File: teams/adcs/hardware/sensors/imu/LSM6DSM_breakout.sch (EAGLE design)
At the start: 6 parts

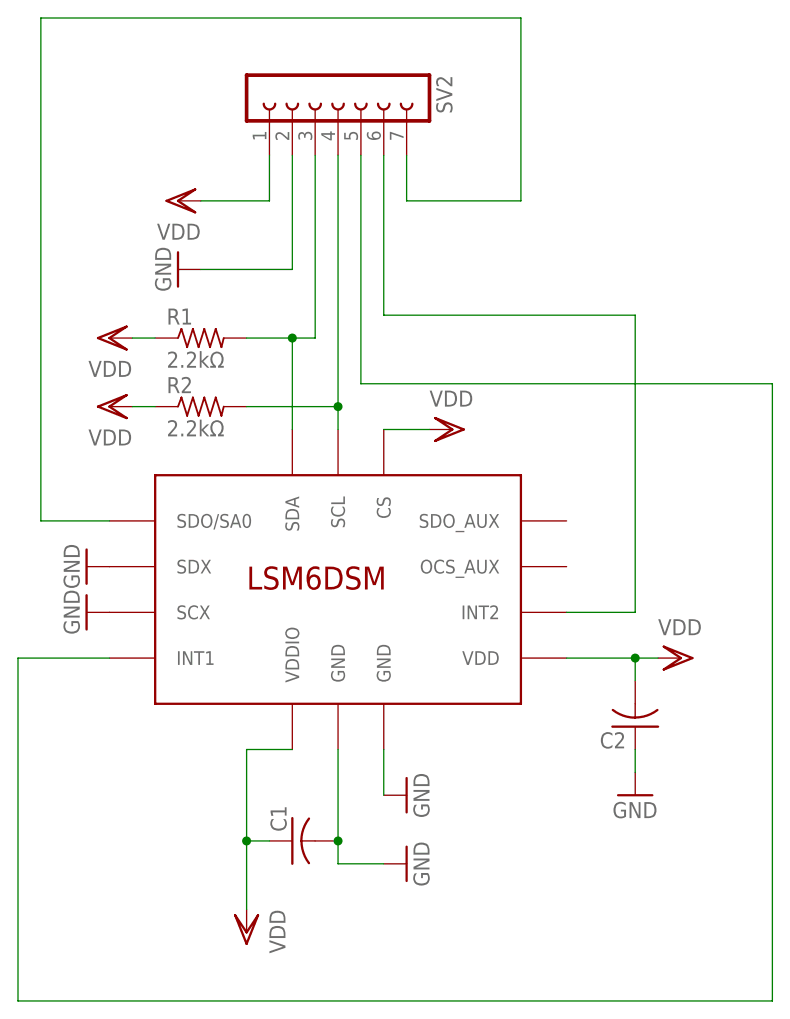
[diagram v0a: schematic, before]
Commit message: ADCS/Sensors: Update eagle version in file header
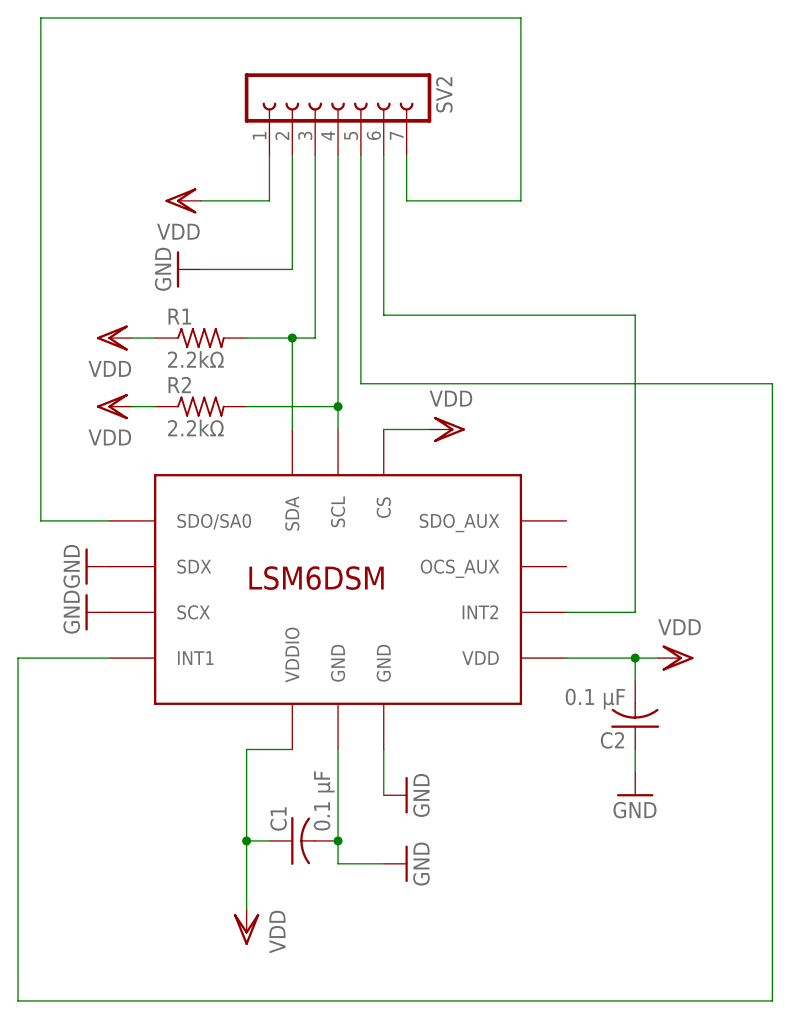
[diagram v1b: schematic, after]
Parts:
- C1, C2: value (none) -> 0.1 μF
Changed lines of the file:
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@@
 <?xml version="1.0" encoding="utf-8"?>
 <!DOCTYPE eagle SYSTEM "eagle.dtd">
-<eagle version="8.2.2">
+<eagle version="8.3.1">
 <drawing>
 <settings>
 <setting alwaysvectorfont="no"/>
+<setting keepoldvectorfont="yes"/>
 <setting verticaltext="up"/>
 </settings>
@@
 <part name="GND2" library="supply1" library_urn="urn:adsk.eagle:library:371" deviceset="GND" device=""/>
 <part name="VDD1" library="supply1" library_urn="urn:adsk.eagle:library:371" deviceset="VDD" device=""/>
-<part name="C1" library="rcl" library_urn="urn:adsk.eagle:library:334" deviceset="C-US" device="C0805"/>
+<part name="C1" library="rcl" library_urn="urn:adsk.eagle:library:334" deviceset="C-US" device="C0805" value="0.1 μF"/>
 <part name="VDD2" library="supply1" library_urn="urn:adsk.eagle:library:371" deviceset="VDD" device=""/>
-<part name="C2" library="rcl" library_urn="urn:adsk.eagle:library:334" deviceset="C-US" device="C0805"/>
+<part name="C2" library="rcl" library_urn="urn:adsk.eagle:library:334" deviceset="C-US" device="C0805" value="0.1 μF"/>
 <part name="GND3" library="supply1" library_urn="urn:adsk.eagle:library:371" deviceset="GND" device=""/>
 <part name="VDD3" library="supply1" library_urn="urn:adsk.eagle:library:371" deviceset="VDD" device=""/>
@@
 <compatibility>
 <note version="8.2" severity="warning">
-Since Version 8.2, Eagle supports online libraries. The ids
+Since Version 8.2, EAGLE supports online libraries. The ids
 of those online libraries will not be understood (or retained)
 with this version.
